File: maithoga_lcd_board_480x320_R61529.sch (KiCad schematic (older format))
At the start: 0 parts

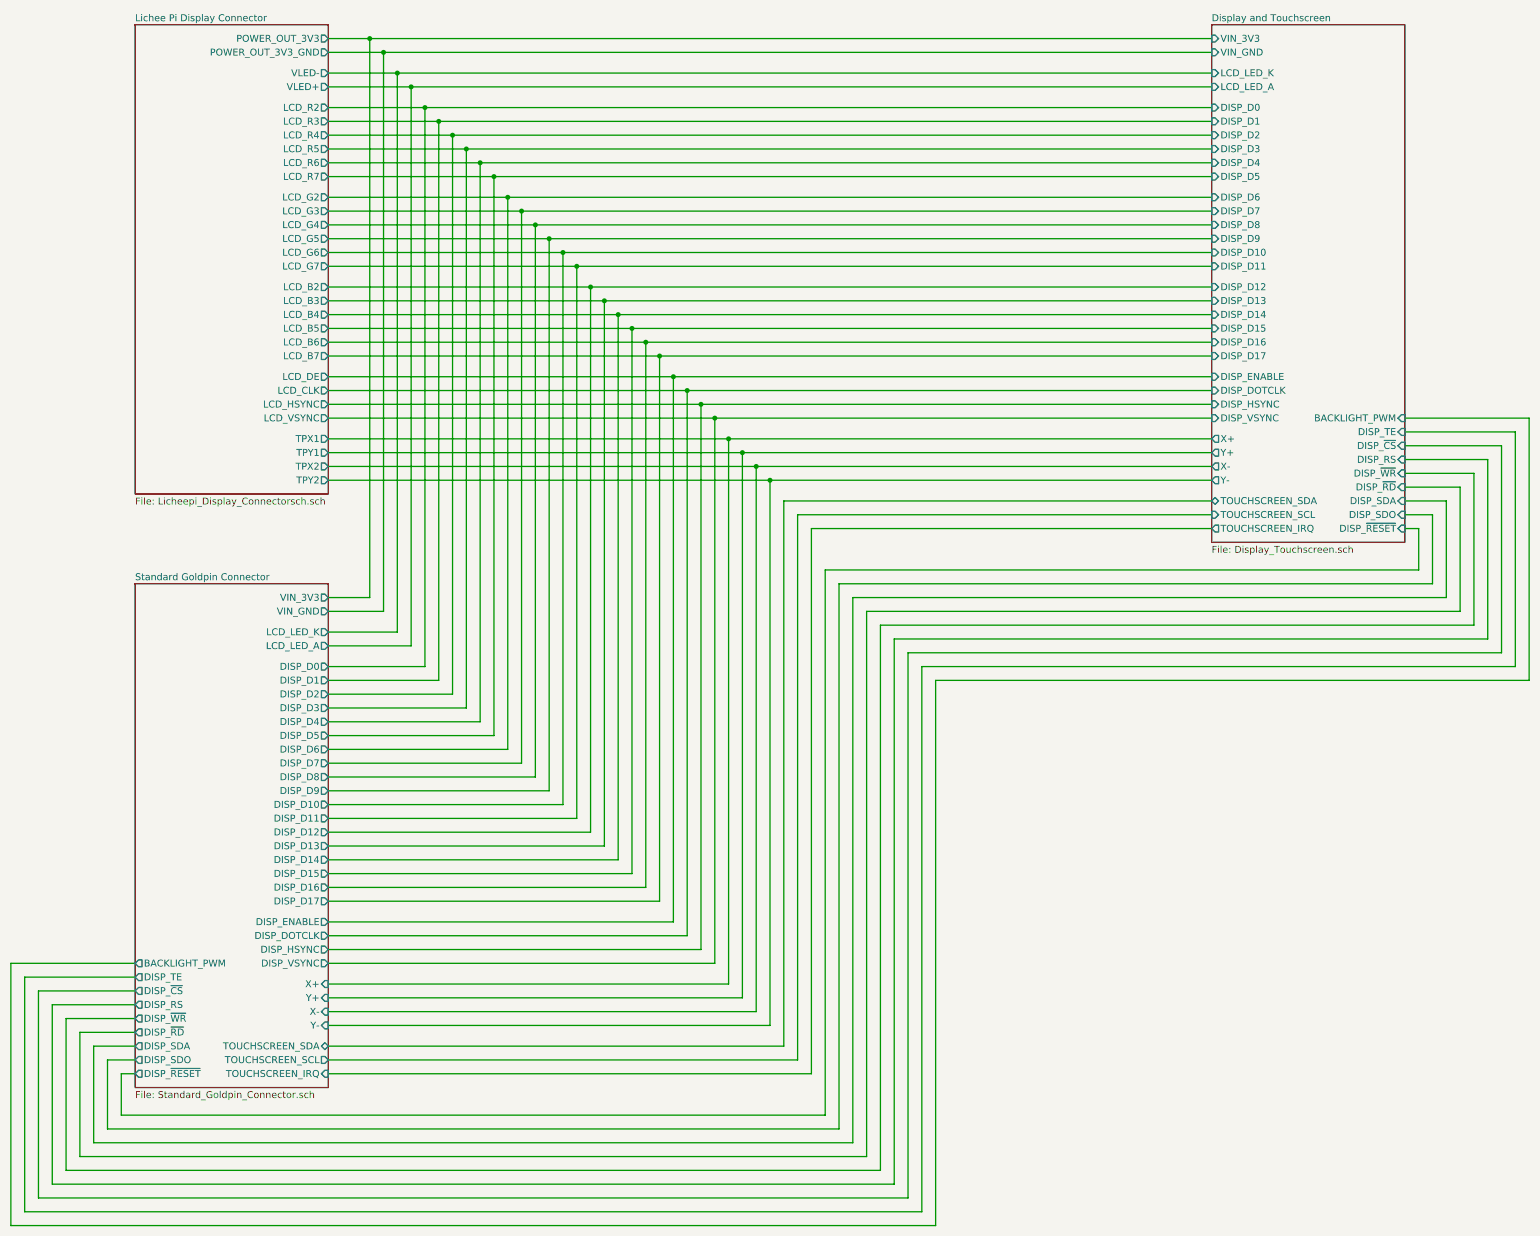
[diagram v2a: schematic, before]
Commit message: Added new capacitive display
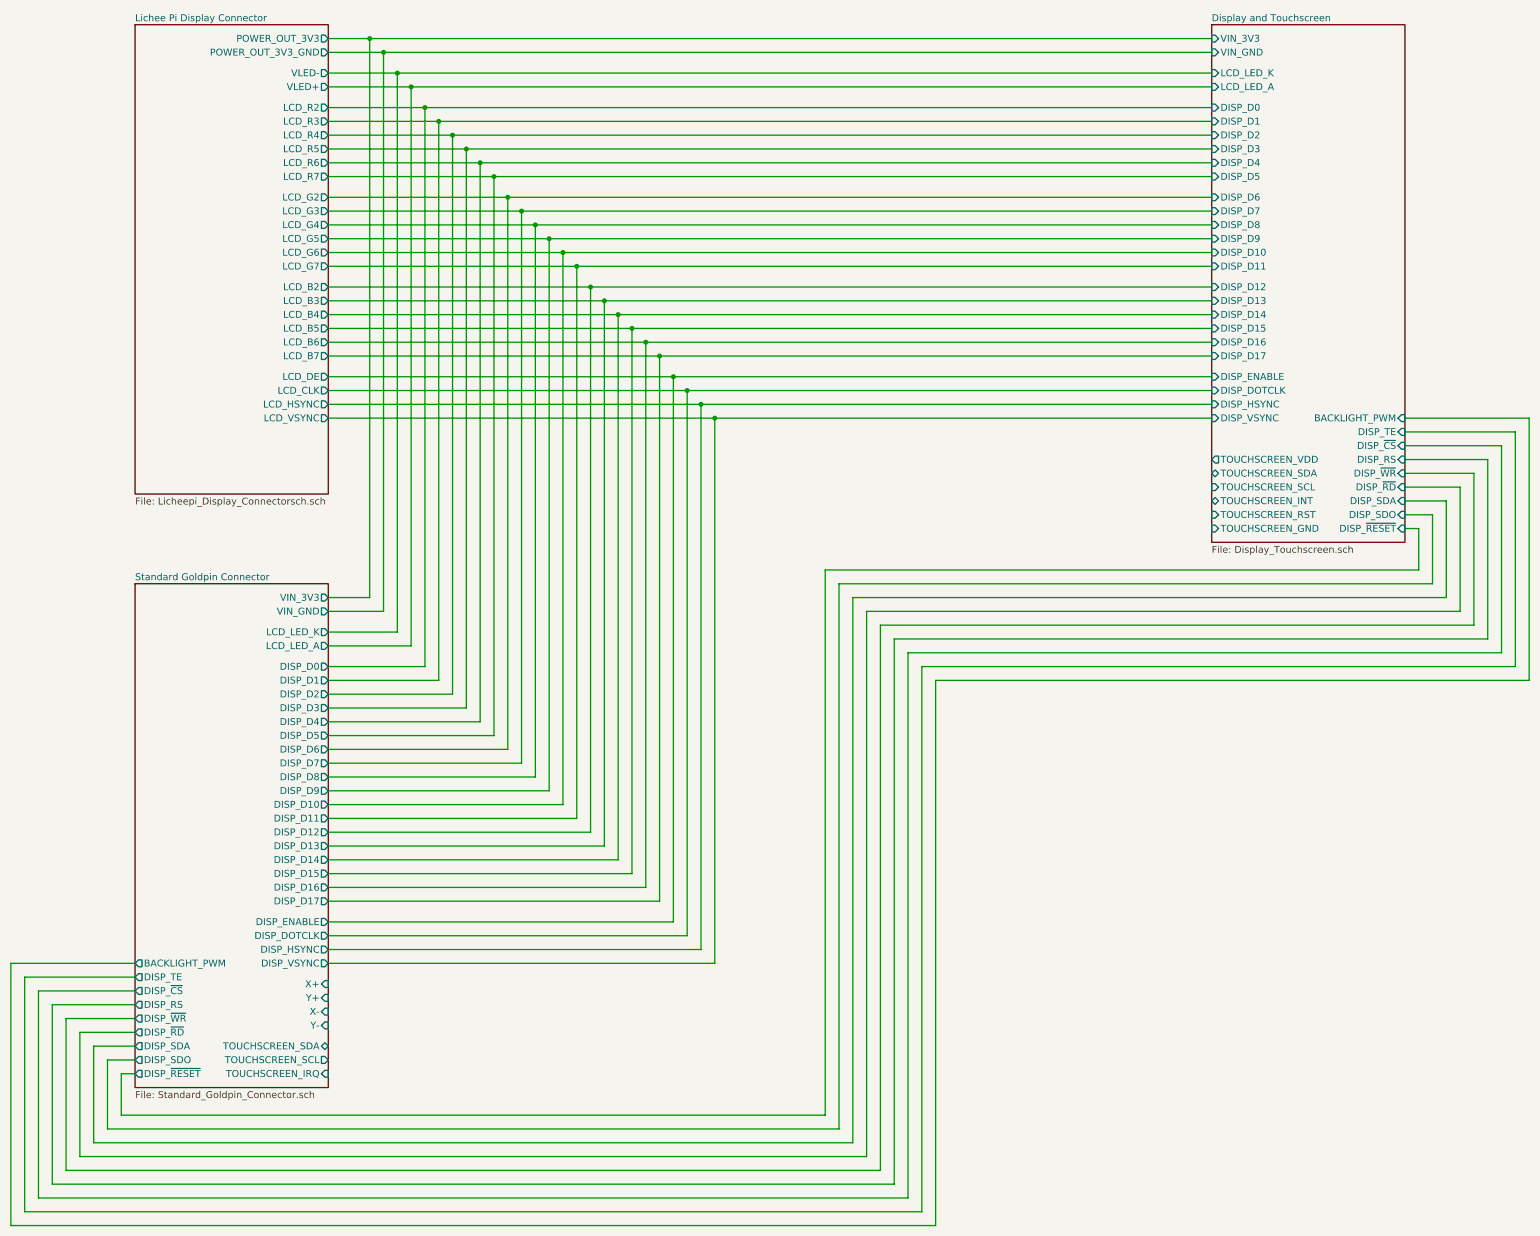
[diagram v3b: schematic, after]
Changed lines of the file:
@@
 encoding utf-8
 Sheet 1 5
-Title "Intermediate board for maithoga lcd 480x320 R61529"
-Date "2020-07-08"
+Title "Intermediate board for maithoga lcd 480x320 R61529 with capacitive TS"
+Date "2020-08-05"
 Rev "V1.0"
 Comp "Embedded System Labs"
@@
 F0 "Display and Touchscreen" 50
 F1 "Display_Touchscreen.sch" 50
-F2 "TOUCHSCREEN_IRQ" O L 11750 5100 50
-F3 "TOUCHSCREEN_SDA" B L 11750 4900 50
-F4 "TOUCHSCREEN_SCL" I L 11750 5000 50
-F5 "VIN_3V3" I L 11750 1550 50
-F6 "VIN_GND" I L 11750 1650 50
-F7 "BACKLIGHT_PWM" I R 13150 4300 50
-F8 "DISP_TE" I R 13150 4400 50
-F9 "DISP_~CS~" I R 13150 4500 50
-F10 "DISP_RS" I R 13150 4600 50
-F11 "DISP_~WR~" I R 13150 4700 50
-F12 "DISP_~RD~" I R 13150 4800 50
-F13 "DISP_SDA" I R 13150 4900 50
-F14 "DISP_SDO" I R 13150 5000 50
-F15 "DISP_D0" I L 11750 2050 50
-F16 "DISP_D1" I L 11750 2150 50
-F17 "DISP_D2" I L 11750 2250 50
-F18 "DISP_D3" I L 11750 2350 50
-F19 "DISP_D4" I L 11750 2450 50
-F20 "DISP_D5" I L 11750 2550 50
-F21 "DISP_D6" I L 11750 2700 50
-F22 "DISP_D7" I L 11750 2800 50
-F23 "DISP_D8" I L 11750 2900 50
-F24 "DISP_D9" I L 11750 3000 50
-F25 "DISP_D10" I L 11750 3100 50
-F26 "DISP_D11" I L 11750 3200 50
-F27 "DISP_D12" I L 11750 3350 50
-F28 "DISP_D13" I L 11750 3450 50
-F29 "DISP_D14" I L 11750 3550 50
-F30 "DISP_D15" I L 11750 3650 50
-F31 "DISP_D16" I L 11750 3750 50
-F32 "DISP_D17" I L 11750 3850 50
-F33 "DISP_ENABLE" I L 11750 4000 50
-F34 "DISP_DOTCLK" I L 11750 4100 50
-F35 "DISP_HSYNC" I L 11750 4200 50
-F36 "DISP_VSYNC" I L 11750 4300 50
-F37 "DISP_~RESET~" I R 13150 5100 50
-F38 "X+" O L 11750 4450 50
-F39 "X-" O L 11750 4650 50
-F40 "Y+" O L 11750 4550 50
-F41 "Y-" O L 11750 4750 50
-F42 "LCD_LED_K" I L 11750 1800 50
-F43 "LCD_LED_A" I L 11750 1900 50
+F2 "VIN_3V3" I L 11750 1550 50
+F3 "VIN_GND" I L 11750 1650 50
+F4 "BACKLIGHT_PWM" I R 13150 4300 50
+F5 "DISP_TE" I R 13150 4400 50
+F6 "DISP_~CS~" I R 13150 4500 50
+F7 "DISP_RS" I R 13150 4600 50
+F8 "DISP_~WR~" I R 13150 4700 50
+F9 "DISP_~RD~" I R 13150 4800 50
+F10 "DISP_SDA" I R 13150 4900 50
+F11 "DISP_SDO" I R 13150 5000 50
+F12 "DISP_D0" I L 11750 2050 50
+F13 "DISP_D1" I L 11750 2150 50
+F14 "DISP_D2" I L 11750 2250 50
+F15 "DISP_D3" I L 11750 2350 50
+F16 "DISP_D4" I L 11750 2450 50
+F17 "DISP_D5" I L 11750 2550 50
+F18 "DISP_D6" I L 11750 2700 50
+F19 "DISP_D7" I L 11750 2800 50
+F20 "DISP_D8" I L 11750 2900 50
+F21 "DISP_D9" I L 11750 3000 50
+F22 "DISP_D10" I L 11750 3100 50
+F23 "DISP_D11" I L 11750 3200 50
+F24 "DISP_D12" I L 11750 3350 50
+F25 "DISP_D13" I L 11750 3450 50
+F26 "DISP_D14" I L 11750 3550 50
+F27 "DISP_D15" I L 11750 3650 50
+F28 "DISP_D16" I L 11750 3750 50
+F29 "DISP_D17" I L 11750 3850 50
+F30 "DISP_ENABLE" I L 11750 4000 50
+F31 "DISP_DOTCLK" I L 11750 4100 50
+F32 "DISP_HSYNC" I L 11750 4200 50
+F33 "DISP_VSYNC" I L 11750 4300 50
+F34 "DISP_~RESET~" I R 13150 5100 50
+F35 "LCD_LED_K" I L 11750 1800 50
+F36 "LCD_LED_A" I L 11750 1900 50
+F37 "TOUCHSCREEN_VDD" O L 11750 4600 50
+F38 "TOUCHSCREEN_SDA" B L 11750 4700 50
+F39 "TOUCHSCREEN_SCL" I L 11750 4800 50
+F40 "TOUCHSCREEN_INT" B L 11750 4900 50
+F41 "TOUCHSCREEN_RST" I L 11750 5000 50
+F42 "TOUCHSCREEN_GND" I L 11750 5100 50
 $EndSheet
 $Sheet
@@
 F24 "LCD_VSYNC" O R 5350 4300 50
 F25 "LCD_DE" O R 5350 4000 50
-F26 "TPX1" O R 5350 4450 50
-F27 "TPY1" O R 5350 4550 50
-F28 "TPX2" O R 5350 4650 50
-F29 "TPY2" O R 5350 4750 50
-F30 "POWER_OUT_3V3" O R 5350 1550 50
-F31 "POWER_OUT_3V3_GND" O R 5350 1650 50
+F26 "POWER_OUT_3V3" O R 5350 1550 50
+F27 "POWER_OUT_3V3_GND" O R 5350 1650 50
 $EndSheet
 Wire Wire Line
@@
 Wire Wire Line
 	11750 4300 8150 4300
-Wire Wire Line
-	5350 4450 8250 4450
-Wire Wire Line
-	11750 4550 8350 4550
-Wire Wire Line
-	5350 4650 8450 4650
-Wire Wire Line
-	11750 4750 8550 4750
 Wire Wire Line
 	5350 5600 5650 5600
@@
 	8150 4300 5350 4300
 Wire Wire Line
-	5350 8400 8250 8400
-Wire Wire Line
-	8250 8400 8250 4450
-Connection ~ 8250 4450
-Wire Wire Line
-	8250 4450 11750 4450
-Wire Wire Line
-	8350 4550 8350 8500
-Wire Wire Line
-	8350 8500 5350 8500
-Connection ~ 8350 4550
-Wire Wire Line
-	8350 4550 5350 4550
-Wire Wire Line
-	5350 8600 8450 8600
-Wire Wire Line
-	8450 8600 8450 4650
-Connection ~ 8450 4650
-Wire Wire Line
-	8450 4650 11750 4650
-Wire Wire Line
-	5350 8700 8550 8700
-Wire Wire Line
-	8550 8700 8550 4750
-Connection ~ 8550 4750
-Wire Wire Line
-	8550 4750 5350 4750
-Wire Wire Line
-	11750 4900 8650 4900
-Wire Wire Line
-	8650 4900 8650 8850
-Wire Wire Line
-	8650 8850 5350 8850
-Wire Wire Line
-	5350 8950 8750 8950
-Wire Wire Line
-	8750 8950 8750 5000
-Wire Wire Line
-	8750 5000 11750 5000
-Wire Wire Line
-	11750 5100 8850 5100
-Wire Wire Line
-	8850 5100 8850 9050
-Wire Wire Line
-	8850 9050 5350 9050
-Wire Wire Line
 	13150 5100 13250 5100

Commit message: Generated gerbers
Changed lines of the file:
@@
 F35 "LCD_LED_K" I L 11750 1800 50
 F36 "LCD_LED_A" I L 11750 1900 50
-F37 "TOUCHSCREEN_VDD" O L 11750 4600 50
+F37 "TOUCHSCREEN_VDD" O L 11750 4400 50
 F38 "TOUCHSCREEN_SDA" B L 11750 4700 50
 F39 "TOUCHSCREEN_SCL" I L 11750 4800 50
-F40 "TOUCHSCREEN_INT" B L 11750 4900 50
-F41 "TOUCHSCREEN_RST" I L 11750 5000 50
-F42 "TOUCHSCREEN_GND" I L 11750 5100 50
+F40 "TOUCHSCREEN_RST" I L 11750 5000 50
+F41 "TOUCHSCREEN_GND" I L 11750 4500 50
+F42 "TOUCHSCREEN_INT" O L 11750 4900 50
 $EndSheet
 $Sheet
@@
 F0 "Standard Goldpin Connector" 50
 F1 "Standard_Goldpin_Connector.sch" 50
-F2 "TOUCHSCREEN_IRQ" I R 5350 9050 50
-F3 "TOUCHSCREEN_SDA" B R 5350 8850 50
-F4 "TOUCHSCREEN_SCL" O R 5350 8950 50
-F5 "VIN_3V3" O R 5350 5600 50
-F6 "VIN_GND" O R 5350 5700 50
-F7 "BACKLIGHT_PWM" O L 3950 8250 50
-F8 "DISP_TE" O L 3950 8350 50
-F9 "DISP_~CS~" O L 3950 8450 50
-F10 "DISP_RS" O L 3950 8550 50
-F11 "DISP_~WR~" O L 3950 8650 50
-F12 "DISP_~RD~" O L 3950 8750 50
-F13 "DISP_SDA" O L 3950 8850 50
-F14 "DISP_SDO" O L 3950 8950 50
-F15 "DISP_D0" O R 5350 6100 50
-F16 "DISP_D1" O R 5350 6200 50
-F17 "DISP_D2" O R 5350 6300 50
-F18 "DISP_D3" O R 5350 6400 50
-F19 "DISP_D4" O R 5350 6500 50
-F20 "DISP_D5" O R 5350 6600 50
-F21 "DISP_D6" O R 5350 6700 50
-F22 "DISP_D7" O R 5350 6800 50
-F23 "DISP_D8" O R 5350 6900 50
-F24 "DISP_D9" O R 5350 7000 50
-F25 "DISP_D10" O R 5350 7100 50
-F26 "DISP_D11" O R 5350 7200 50
-F27 "DISP_D12" O R 5350 7300 50
-F28 "DISP_D13" O R 5350 7400 50
-F29 "DISP_D14" O R 5350 7500 50
-F30 "DISP_D15" O R 5350 7600 50
-F31 "DISP_D16" O R 5350 7700 50
-F32 "DISP_D17" O R 5350 7800 50
-F33 "DISP_ENABLE" O R 5350 7950 50
-F34 "DISP_DOTCLK" O R 5350 8050 50
-F35 "DISP_HSYNC" O R 5350 8150 50
-F36 "DISP_VSYNC" O R 5350 8250 50
-F37 "DISP_~RESET~" O L 3950 9050 50
-F38 "LCD_LED_K" O R 5350 5850 50
-F39 "LCD_LED_A" O R 5350 5950 50
-F40 "X-" I R 5350 8600 50
-F41 "X+" I R 5350 8400 50
-F42 "Y-" I R 5350 8700 50
-F43 "Y+" I R 5350 8500 50
+F2 "VIN_3V3" O R 5350 5600 50
+F3 "VIN_GND" O R 5350 5700 50
+F4 "BACKLIGHT_PWM" O L 3950 8250 50
+F5 "DISP_TE" O L 3950 8350 50
+F6 "DISP_~CS~" O L 3950 8450 50
+F7 "DISP_RS" O L 3950 8550 50
+F8 "DISP_~WR~" O L 3950 8650 50
+F9 "DISP_~RD~" O L 3950 8750 50
+F10 "DISP_SDA" O L 3950 8850 50
+F11 "DISP_SDO" O L 3950 8950 50
+F12 "DISP_D0" O R 5350 6100 50
+F13 "DISP_D1" O R 5350 6200 50
+F14 "DISP_D2" O R 5350 6300 50
+F15 "DISP_D3" O R 5350 6400 50
+F16 "DISP_D4" O R 5350 6500 50
+F17 "DISP_D5" O R 5350 6600 50
+F18 "DISP_D6" O R 5350 6700 50
+F19 "DISP_D7" O R 5350 6800 50
+F20 "DISP_D8" O R 5350 6900 50
+F21 "DISP_D9" O R 5350 7000 50
+F22 "DISP_D10" O R 5350 7100 50
+F23 "DISP_D11" O R 5350 7200 50
+F24 "DISP_D12" O R 5350 7300 50
+F25 "DISP_D13" O R 5350 7400 50
+F26 "DISP_D14" O R 5350 7500 50
+F27 "DISP_D15" O R 5350 7600 50
+F28 "DISP_D16" O R 5350 7700 50
+F29 "DISP_D17" O R 5350 7800 50
+F30 "DISP_ENABLE" O R 5350 7950 50
+F31 "DISP_DOTCLK" O R 5350 8050 50
+F32 "DISP_HSYNC" O R 5350 8150 50
+F33 "DISP_VSYNC" O R 5350 8250 50
+F34 "DISP_~RESET~" O L 3950 9050 50
+F35 "LCD_LED_K" O R 5350 5850 50
+F36 "LCD_LED_A" O R 5350 5950 50
+F37 "TOUCHSCREEN_IRQ" I R 5350 8750 50
+F38 "TOUCHSCREEN_SDA" B R 5350 8550 50
+F39 "TOUCHSCREEN_SCL" O R 5350 8650 50
+F40 "TOUCHSCREEN_RESET" O R 5350 8850 50
 $EndSheet
 $Sheet
-S 3950 1450 1400 3400
+S 3950 1450 1400 2950
 U 5F06906E
 F0 "Lichee Pi Display Connector" 50
@@
 Wire Wire Line
 	5350 5600 5650 5600
-Wire Wire Line
-	5650 5600 5650 1550
 Connection ~ 5650 1550
 Wire Wire Line
 	5650 1550 11750 1550
 Wire Wire Line
-	5750 1650 5750 5700
+	5750 1650 5750 4500
 Wire Wire Line
 	5750 5700 5350 5700
@@
 	13250 5100 13250 5400
 Wire Wire Line
-	8950 5400 8950 9350
-Wire Wire Line
-	8950 9350 3850 9350
+	9650 5400 9650 9350
+Wire Wire Line
+	9650 9350 3850 9350
 Wire Wire Line
 	3850 9350 3850 9050
@@
 	3850 9050 3950 9050
 Wire Wire Line
-	8950 5400 13250 5400
+	9650 5400 13250 5400
 Wire Wire Line
 	13150 5000 13350 5000
@@
 	13350 5000 13350 5500
 Wire Wire Line
-	13350 5500 9050 5500
-Wire Wire Line
-	9050 5500 9050 9450
-Wire Wire Line
-	9050 9450 3750 9450
+	13350 5500 9750 5500
+Wire Wire Line
+	9750 5500 9750 9450
+Wire Wire Line
+	9750 9450 3750 9450
 Wire Wire Line
 	3750 9450 3750 8950
@@
 	13450 4900 13450 5600
 Wire Wire Line
-	13450 5600 9150 5600
-Wire Wire Line
-	9150 5600 9150 9550
-Wire Wire Line
-	9150 9550 3650 9550
+	13450 5600 9850 5600
+Wire Wire Line
+	9850 5600 9850 9550
+Wire Wire Line
+	9850 9550 3650 9550
 Wire Wire Line
 	3650 9550 3650 8850
@@
 	13550 4800 13550 5700
 Wire Wire Line
-	13550 5700 9250 5700
-Wire Wire Line
-	9250 5700 9250 9650
-Wire Wire Line
-	9250 9650 3550 9650
+	13550 5700 9950 5700
+Wire Wire Line
+	9950 5700 9950 9650
+Wire Wire Line
+	9950 9650 3550 9650
 Wire Wire Line
 	3550 9650 3550 8750
@@
 	13650 4700 13650 5800
 Wire Wire Line
-	13650 5800 9350 5800
-Wire Wire Line
-	9350 5800 9350 9750
-Wire Wire Line
-	9350 9750 3450 9750
+	13650 5800 10050 5800
+Wire Wire Line
+	10050 5800 10050 9750
+Wire Wire Line
+	10050 9750 3450 9750
 Wire Wire Line
 	3450 9750 3450 8650
@@
 	13750 4600 13750 5900
 Wire Wire Line
-	13750 5900 9450 5900
-Wire Wire Line
-	9450 5900 9450 9850
-Wire Wire Line
-	9450 9850 3350 9850
+	13750 5900 10150 5900
+Wire Wire Line
+	10150 5900 10150 9850
+Wire Wire Line
+	10150 9850 3350 9850
 Wire Wire Line
 	3350 9850 3350 8550
@@
 	13850 4500 13850 6000
 Wire Wire Line
-	13850 6000 9550 6000
-Wire Wire Line
-	9550 6000 9550 9950
-Wire Wire Line
-	9550 9950 3250 9950
+	13850 6000 10250 6000
+Wire Wire Line
+	10250 6000 10250 9950
+Wire Wire Line
+	10250 9950 3250 9950
 Wire Wire Line
 	3250 9950 3250 8450
@@
 	13950 4400 13950 6100
 Wire Wire Line
-	13950 6100 9650 6100
-Wire Wire Line
-	9650 6100 9650 10050
-Wire Wire Line
-	9650 10050 3150 10050
+	13950 6100 10350 6100
+Wire Wire Line
+	10350 6100 10350 10050
+Wire Wire Line
+	10350 10050 3150 10050
 Wire Wire Line
 	3150 10050 3150 8350
@@
 	14050 4300 14050 6200
 Wire Wire Line
-	14050 6200 9750 6200
-Wire Wire Line
-	9750 6200 9750 10150
-Wire Wire Line
-	9750 10150 3050 10150
+	14050 6200 10450 6200
+Wire Wire Line
+	10450 6200 10450 10150
+Wire Wire Line
+	10450 10150 3050 10150
 Wire Wire Line
 	3050 10150 3050 8250
 Wire Wire Line
 	3050 8250 3950 8250
+Wire Wire Line
+	11750 4400 5650 4400
+Connection ~ 5650 4400
+Wire Wire Line
+	5650 4400 5650 1550
+Wire Wire Line
+	11750 4500 5750 4500
+Connection ~ 5750 4500
+Wire Wire Line
+	5350 8550 8700 8550
+Wire Wire Line
+	8700 8550 8700 4700
+Wire Wire Line
+	8700 4700 11750 4700
+Wire Wire Line
+	11750 4800 8800 4800
+Wire Wire Line
+	8800 4800 8800 8650
+Wire Wire Line
+	8800 8650 5350 8650
+Wire Wire Line
+	5350 8750 8900 8750
+Wire Wire Line
+	8900 8750 8900 4900
+Wire Wire Line
+	8900 4900 11750 4900
+Wire Wire Line
+	11750 5000 9000 5000
+Wire Wire Line
+	9000 5000 9000 8850
+Wire Wire Line
+	9000 8850 5350 8850
+Wire Wire Line
+	5650 4400 5650 5600
+Wire Wire Line
+	5750 4500 5750 5700
 $EndSCHEMATC
